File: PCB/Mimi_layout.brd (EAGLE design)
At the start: 39 x 54.6 mm, 13 parts

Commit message: Layout V2
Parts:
- added C1: 10uF, SparkFun:EIA3216
- added C2: 68uF, SparkFun:EIA3528
- added D1: MBRA140, SparkFun:SMA-DIODE
- added L1: 47uH, SparkFun:CR54
- added R1: 1K, resistor:R0805
- added R2: 1.56k, resistor:R0805
- added U1: NCP1402, SparkFun:SOT23-5
- added U2: V_REG_317SMD, SparkFun-PowerIC:SOT223
- moved R13 25.7 mm to (63.5, 11.4), turned to 270 degrees
- moved EC4-500 18.5 mm to (72.4, 47.0), turned to 90 degrees
- moved SHINYEI 14.0 mm to (71.1, 34.3), turned to 90 degrees
- moved FAN 11.5 mm to (40.6, 21.6), turned to 0 degrees
- moved R11 9.16 mm to (53.3, 24.1)
- moved MKR1000_RIGHT 7.62 mm to (47.0, 41.9)
- moved MKR1000_LEFT 5.08 mm to (26.7, 41.9)
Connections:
- removed net MKR_GND: MKR1000_LEFT.4
- new net N$2: R1.1, R2.2, U2.1
- new net N$3: D1.A, L1.P$2, U1.5
- new net PM_OUT: SHINYEI.1, U2.3
- new net V_5: C2.A, D1.C, EC4-500.1, FAN.1, SHINYEI.2, U1.1, U1.2
- net GND: now also C1.C, C2.C, FAN.2, MKR1000_LEFT.4, R2.1, U1.4
- net MKR_0: now also R1.2, U2.2; no longer SHINYEI.1
- net MKR_5V: no longer EC4-500.1, FAN.1, SHINYEI.2
- net MKR_VCC: now also C1.A, L1.P$1
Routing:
- net V_5: track 0.00 -> 77.3 mm, vias 0 -> 2
- net MKR_5V: track 76.8 -> 0.00 mm, vias 2 -> 0
- net MKR_VCC: track 16.8 -> 66.5 mm
- net PM_OUT: track 0.00 -> 45.9 mm, vias 0 -> 2
- net MKR_0: track 27.2 -> 9.65 mm, vias 2 -> 0
- net N$2: track 0.00 -> 11.5 mm
- net N$3: track 0.00 -> 9.86 mm
- net MKR_A3: track 21.6 -> 30.1 mm
- net MKR_A1: track 15.9 -> 9.71 mm
- net MKR_12_SCL: track 47.1 -> 42.0 mm
- net V_3.3: track 41.5 -> 38.1 mm
- net MICS_2: track 17.7 -> 20.0 mm, vias 0 -> 2
- net MKR_11_SDA: track 36.8 -> 38.2 mm, vias 1 -> 2
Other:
- board size 39 x 54.6 mm -> 51.7 x 54.6 mm

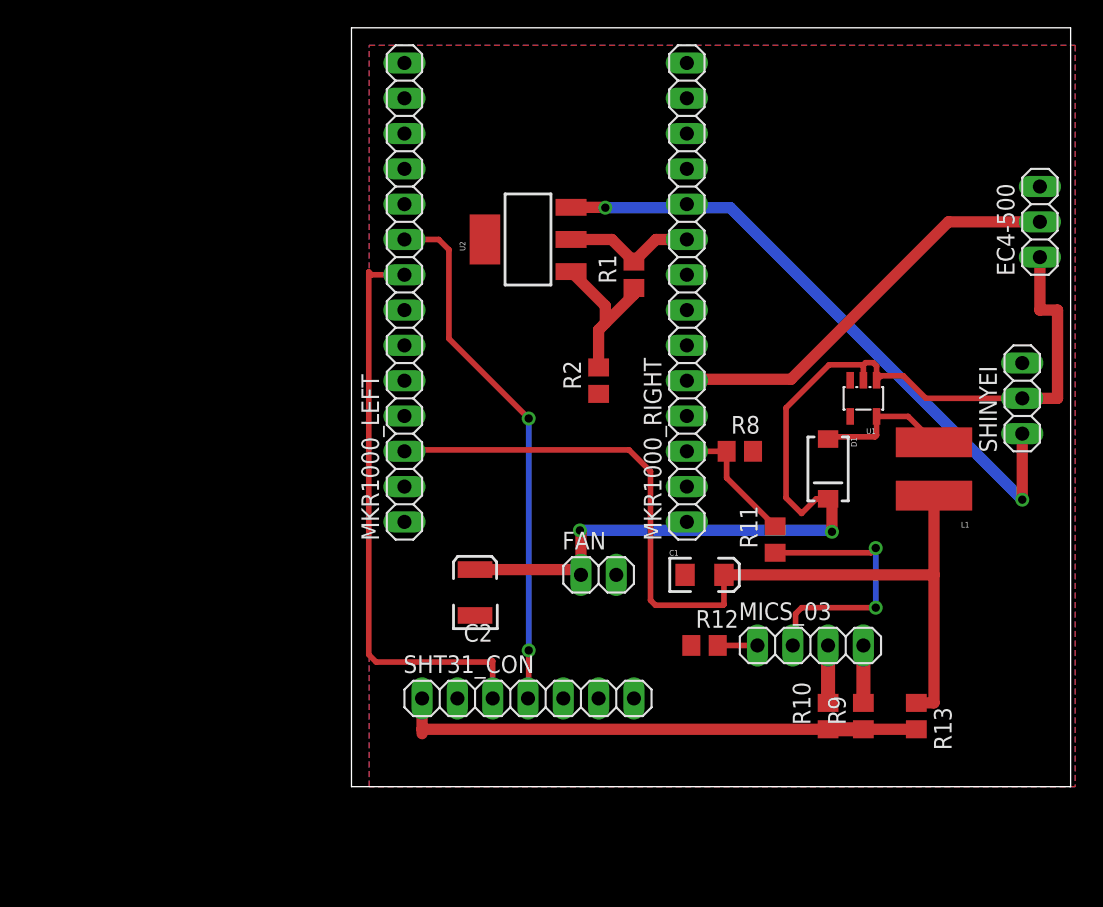
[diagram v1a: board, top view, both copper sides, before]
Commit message: Board V3
Version 3 of the schematic and board. might be able to shrink a little more but everything is pretty tight as is.
Also added EPL LPKF CAM/DRU files for making GBRs for manufacturing and ensuring the layout does not violate machine tolerances
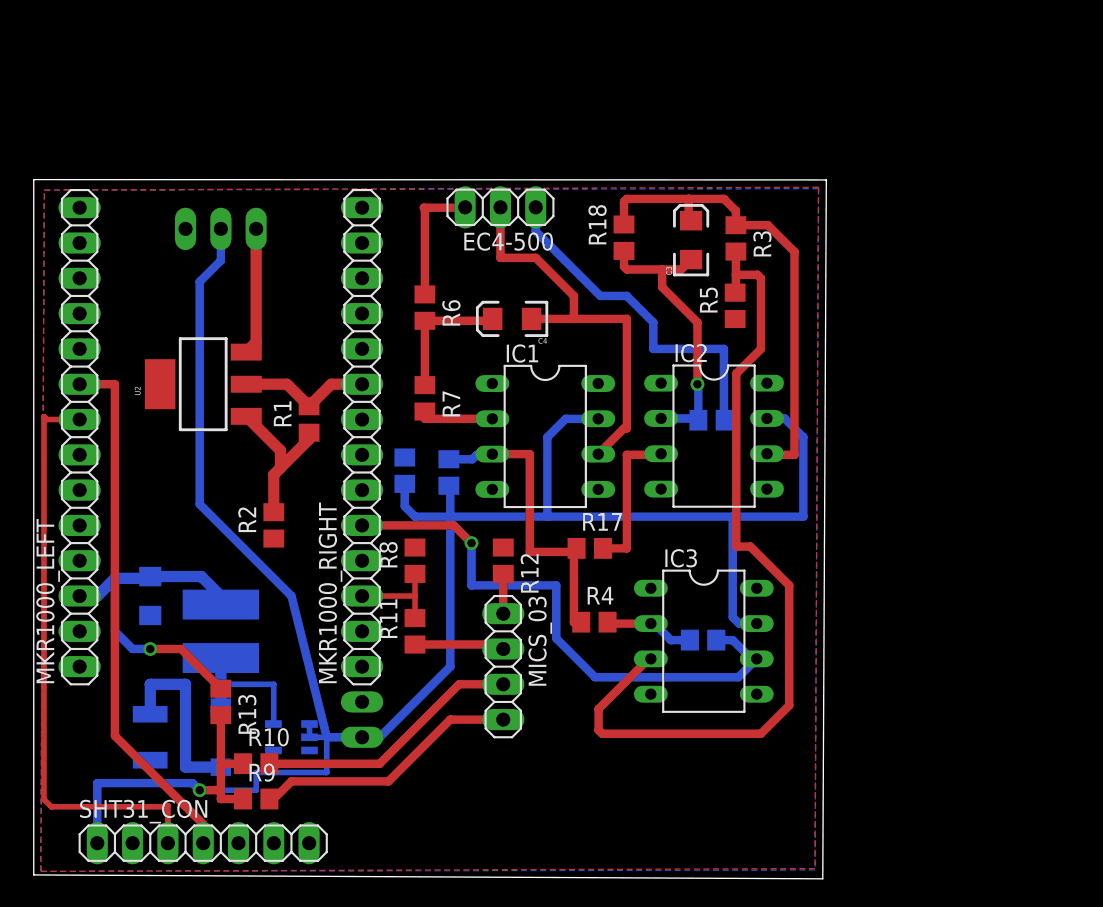
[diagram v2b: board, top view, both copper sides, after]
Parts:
- added C3, C4: 100nf, SparkFun:EIA3216
- added IC1, IC2, IC3: AD820N, analog-devices:DIL08
- added R14, R15, R18, R6, R7: 10k, resistor:R0805
- added R16, R17: 10, resistor:R0805
- added R19, R3, R4, R5: 330, resistor:R0805
- moved SHINYEI 58.9 mm to (13.5, 46.5), flipped to the bottom, turned to 0 degrees
- moved L1 52.6 mm to (13.5, 17.5), flipped to the bottom, turned to 0 degrees
- moved R13 50.0 mm to (13.5, 12.4)
- moved U1 47.8 mm to (18.5, 9.91), flipped to the bottom, turned to 270 degrees
- moved D1 47.8 mm to (13.5, 9.91), flipped to the bottom
- moved R9 44.1 mm to (16.0, 5.46), turned to 0 degrees
- moved R10 41.3 mm to (16.0, 8.00), turned to 0 degrees
- moved C1 39.9 mm to (8.38, 20.1), flipped to the bottom, turned to 90 degrees
- moved EC4-500 38.8 mm to (33.6, 48.0), turned to 180 degrees
- moved R11 26.7 mm to (27.4, 17.5)
- moved C2 25.6 mm to (8.38, 9.91), flipped to the bottom
- moved MKR1000_LEFT 25.6 mm to (3.30, 31.5)
- moved MKR1000_RIGHT 25.6 mm to (23.6, 31.5)
- moved R2 25.6 mm to (17.3, 25.1)
- moved SHT31_CON 25.6 mm to (12.2, 2.29)
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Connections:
- new net CO_C: C4.C, EC4-500.2, IC1.6
- new net CO_R: EC4-500.3, R6.1
- new net CO_S: EC4-500.1, R16.2
- new net N$10: IC3.3, R3.2, R5.2
- new net N$11: IC3.2, R19.1, R4.2
- new net N$4: C4.A, R6.2, R7.1
- new net N$5: IC1.3, R14.2, R17.1, R4.1
- new net N$6: IC1.2, R7.2
- new net N$7: IC2.3, R17.2
- new net N$8: C3.C, IC2.2, R16.1, R18.1
- new net N$9: C3.A, IC2.6, R18.2, R3.1
- net GND: now also IC1.4, IC2.4, IC3.4, R15.1, R5.1; no longer EC4-500.3
- net MKR_A3: now also IC3.6, R19.2; no longer EC4-500.2
- net V_5: now also IC1.7, IC2.7, IC3.7, R14.1, R15.2; no longer EC4-500.1
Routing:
- net V_5: track 77.3 -> 151.4 mm, vias 2 -> 0
- net N$10: track 0.00 -> 60.0 mm
- net MKR_VCC: track 66.5 -> 25.1 mm, vias 0 -> 1
- net PM_OUT: track 45.9 -> 8.91 mm, vias 2 -> 0
- net N$9: track 0.00 -> 34.4 mm
- net CO_C: track 0.00 -> 29.3 mm
- net CO_S: track 0.00 -> 25.0 mm
- net N$5: track 0.00 -> 22.3 mm
- net N$8: track 0.00 -> 20.9 mm, vias 0 -> 1
- net V_3.3: track 38.1 -> 22.6 mm, vias 0 -> 1
- net MICS_4: track 4.13 -> 19.2 mm
- net MICS_3: track 4.13 -> 19.2 mm
- net MICS_2: track 20.0 -> 6.67 mm, vias 2 -> 0
- net N$7: track 0.00 -> 11.0 mm
- net MKR_A3: track 30.1 -> 41.0 mm, vias 0 -> 1
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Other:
- board size 51.7 x 54.6 mm -> 57 x 50.3 mm

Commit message: compression & schematic fixes
board dimensions shrunk to 2.18 * 1.62. will try to compress further but from this point on there will be diminishing returns on time spent vs   resulting compression.

also fixed a few warnings in schematic capture mode. there are still some but none are serious problems.
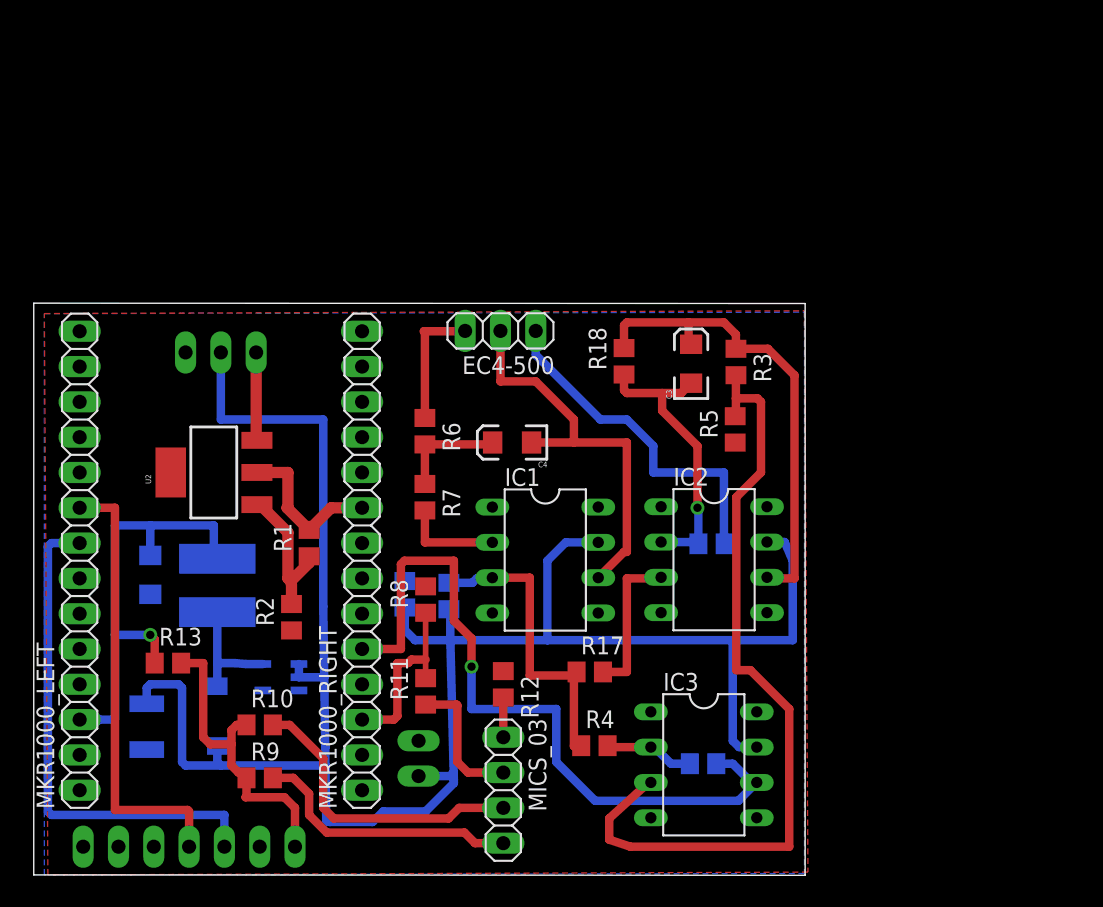
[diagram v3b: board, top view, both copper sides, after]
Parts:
- moved C4 8.89 mm to (34.4, 31.1)
- moved R16 8.89 mm to (48.8, 23.8)
- moved R12 8.89 mm to (33.8, 13.7)
- moved EC4-500 8.89 mm to (33.6, 39.1)
- moved IC1 8.89 mm to (36.8, 22.7)
- moved IC3 8.89 mm to (48.2, 7.92)
- moved MICS_03 8.89 mm to (33.8, 6.10)
- moved R14 8.89 mm to (29.9, 20.1)
- moved R17 8.89 mm to (40.0, 14.6)
- moved R18 8.89 mm to (42.5, 37.0)
- moved R3 8.89 mm to (50.5, 36.9)
- moved R5 8.89 mm to (50.5, 32.1)
- moved SHINYEI 8.89 mm to (13.5, 37.6)
- moved R19 8.89 mm to (48.2, 8.00)
- moved R4 8.89 mm to (40.3, 9.30)
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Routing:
- net MKR_A3: track 41.0 -> 53.5 mm
- net MKR_VCC: track 25.1 -> 33.0 mm
- net MKR_A1: track 6.99 -> 13.3 mm
- net MKR_11_SDA: track 38.2 -> 32.2 mm
- net MKR_12_SCL: track 42.0 -> 36.5 mm
- net MICS_2: track 6.67 -> 10.3 mm
- net V_5: track 151.4 -> 148.3 mm
- net PM_OUT: track 8.91 -> 6.09 mm
- net MICS_3: track 19.2 -> 21.8 mm
- net MKR_0: track 9.65 -> 11.5 mm
- net N$4: track 9.64 -> 7.86 mm
- net N$6: track 5.37 -> 7.15 mm
- net N$3: track 10.3 -> 8.60 mm
- net N$10: track 60.0 -> 58.4 mm
- net N$2: track 11.5 -> 10.6 mm
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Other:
- board size 57 x 50.3 mm -> 55.5 x 41.2 mm

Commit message: capacitor fix
removed oversize capacitors (1206) and replaced with 0805s
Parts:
- removed C1: 10uF, SparkFun:EIA3216
- removed C2: 68uF, SparkFun:EIA3528
- removed C3, C4: 100nf, SparkFun:EIA3216
- added C5, C8: 100nf, resistor:C0805
- added C6: 68uf, resistor:C0805
- added C9: 10uf, resistor:C0805
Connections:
- net CO_C: now also C5.2; no longer C4.C
- net GND: now also C6.2, C9.2; no longer C1.C, C2.C
- net MKR_VCC: now also C9.1; no longer C1.A
- net N$4: now also C5.1; no longer C4.A
- net N$8: now also C8.2; no longer C3.C
- net N$9: now also C8.1; no longer C3.A
- net V_3.3: no longer R10.1, R9.1
- net V_5: now also C6.1, R10.1, R9.1; no longer C2.A
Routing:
- net V_5: track 148.3 -> 155.1 mm, vias 0 -> 1
- net V_3.3: track 22.5 -> 20.5 mm
- net N$4: track 7.86 -> 9.33 mm
- net N$8: track 20.9 -> 21.7 mm
- net CO_C: track 29.3 -> 28.6 mm

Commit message: replaced components, rerouted
a few components were removed and resistances changed in accordance with observed device behavior
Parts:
- removed U2: V_REG_317SMD, SparkFun-PowerIC:SOT223
- R1: value 1K -> 22K
- R2: value 1.56k -> 68K
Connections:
- removed net N$2: R1.1, R2.2, U2.1
- net MKR_0: now also R1.1, R2.2; no longer R1.2, U2.2
- net PM_OUT: now also R1.2; no longer U2.3
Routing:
- net N$2: track 10.6 -> 0.00 mm
- net PM_OUT: track 6.09 -> 14.3 mm
- net MKR_0: track 11.5 -> 13.9 mm
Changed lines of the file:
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@@
 <element name="D1" library="SparkFun" package="SMA-DIODE" value="MBRA140" x="13.208" y="11.43" rot="MR270"/>
 <element name="L1" library="SparkFun" package="CR54" value="47uH" x="13.208" y="20.828" rot="MR0"/>
-<element name="U2" library="SparkFun-PowerIC" package="SOT223" value="V_REG_317SMD" x="12.954" y="28.956" rot="R90"/>
-<element name="R1" library="resistor" package="R0805" value="1K" x="19.812" y="23.876" rot="R90"/>
-<element name="R2" library="resistor" package="R0805" value="1.56k" x="18.542" y="18.542" rot="R90"/>
+<element name="R1" library="resistor" package="R0805" value="22K" x="19.812" y="23.876" rot="R90"/>
+<element name="R2" library="resistor" package="R0805" value="68K" x="18.542" y="18.542" rot="R90"/>
 <element name="IC1" library="analog-devices" package="DIL08" value="AD820N" x="36.8046" y="22.6568" rot="R270">
 <attribute name="MPN" value="" x="36.8046" y="22.6568" size="1.778" layer="27" rot="R270" display="off"/>
@@
 <signal name="MKR_0">
 <contactref element="MKR1000_RIGHT" pad="9"/>
-<contactref element="U2" pad="2"/>
-<contactref element="R1" pad="2"/>
 <wire x1="23.622" y1="26.416" x2="21.402" y2="26.416" width="0.8128" layer="1"/>
-<wire x1="21.402" y1="26.416" x2="19.812" y2="24.826" width="0.8128" layer="1"/>
-<wire x1="19.812" y1="24.826" x2="18.222" y2="26.416" width="0.8128" layer="1"/>
-<wire x1="16.0528" y1="28.956" x2="18.288" y2="28.956" width="0.8128" layer="1"/>
-<wire x1="18.288" y1="28.956" x2="18.288" y2="26.482" width="0.8128" layer="1"/>
-<wire x1="18.288" y1="26.482" x2="18.222" y2="26.416" width="0.8128" layer="1"/>
+<contactref element="R1" pad="1"/>
+<contactref element="R2" pad="2"/>
+<wire x1="18.542" y1="20.9296" x2="18.542" y2="19.492" width="0.8128" layer="1"/>
+<wire x1="19.812" y1="22.926" x2="19.812" y2="22.4536" width="0.8128" layer="1"/>
+<wire x1="19.812" y1="22.4536" x2="18.9992" y2="21.6408" width="0.8128" layer="1"/>
+<wire x1="18.9992" y1="21.6408" x2="18.4912" y2="21.1328" width="0.8128" layer="1"/>
+<wire x1="18.4912" y1="21.1328" x2="18.542" y2="20.9296" width="0.8128" layer="1"/>
+<wire x1="21.402" y1="26.416" x2="21.402" y2="21.91" width="0.8128" layer="1"/>
+<wire x1="21.402" y1="21.91" x2="20.32" y2="20.828" width="0.8128" layer="1"/>
+<wire x1="20.32" y1="20.828" x2="19.812" y2="20.828" width="0.8128" layer="1"/>
+<wire x1="19.812" y1="20.828" x2="18.9992" y2="21.6408" width="0.8128" layer="1"/>
 </signal>
 <signal name="MKR_1">
@@
 <wire x1="8.128" y1="11.872" x2="8.128" y2="13.462" width="0.6096" layer="16"/>
 </signal>
-<signal name="N$2">
-<contactref element="R1" pad="1"/>
-<contactref element="U2" pad="1"/>
-<contactref element="R2" pad="2"/>
-<wire x1="18.542" y1="20.9296" x2="18.542" y2="19.492" width="0.8128" layer="1"/>
-<wire x1="19.812" y1="22.926" x2="19.812" y2="22.4536" width="0.8128" layer="1"/>
-<wire x1="19.812" y1="22.4536" x2="18.4912" y2="21.1328" width="0.8128" layer="1"/>
-<wire x1="18.4912" y1="21.1328" x2="18.542" y2="20.9296" width="0.8128" layer="1"/>
-<wire x1="16.0528" y1="26.6446" x2="16.2814" y2="26.6446" width="0.8128" layer="1"/>
-<wire x1="16.2814" y1="26.6446" x2="18.288" y2="24.638" width="0.8128" layer="1"/>
-<wire x1="18.288" y1="24.638" x2="18.288" y2="21.336" width="0.8128" layer="1"/>
-<wire x1="18.288" y1="21.336" x2="18.4912" y2="21.1328" width="0.8128" layer="1"/>
-</signal>
 <signal name="PM_OUT">
 <contactref element="SHINYEI" pad="1"/>
-<contactref element="U2" pad="3"/>
-<wire x1="16.002" y1="37.338" x2="16.002" y2="31.3182" width="0.8128" layer="1"/>
-<wire x1="16.002" y1="31.3182" x2="16.0528" y2="31.2674" width="0.8128" layer="1"/>
-<wire x1="16.002" y1="37.338" x2="16.002" y2="37.592" width="0" layer="19" extent="1-1"/>
+<contactref element="R1" pad="2"/>
+<wire x1="16.002" y1="37.592" x2="16.002" y2="30.226" width="0.8128" layer="1"/>
+<wire x1="16.002" y1="30.226" x2="19.812" y2="26.416" width="0.8128" layer="1"/>
+<wire x1="19.812" y1="26.416" x2="19.812" y2="24.826" width="0.8128" layer="1"/>
 </signal>
 <signal name="CO_C">
